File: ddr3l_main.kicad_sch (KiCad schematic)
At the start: 1 part

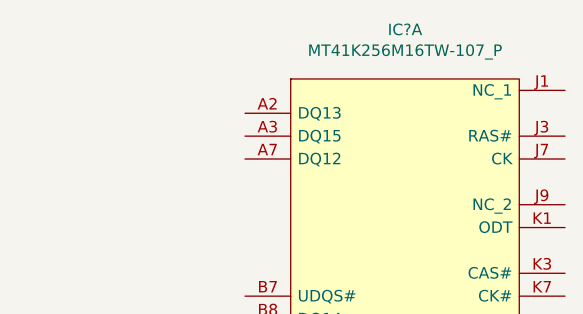
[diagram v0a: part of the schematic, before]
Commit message: Annotate symbols on ddr3l page
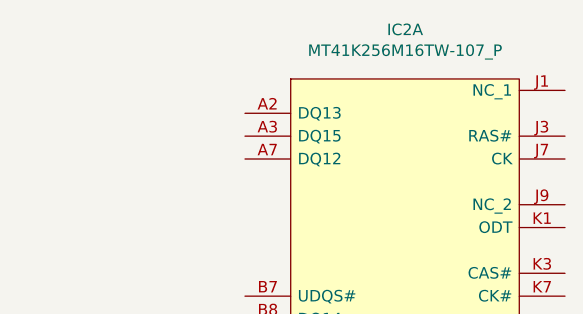
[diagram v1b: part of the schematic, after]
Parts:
- gave numbers to parts that had none: 1
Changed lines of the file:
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@@
 		(on_board yes)
 		(dnp no)
-		(property "Reference" "IC?"
+		(property "Reference" "IC2"
 			(at 99.06 35.179 0)
 			(effects
@@
 			(project "Simple_SDR"
 				(path "/006caa78-17ed-4ca3-959e-671c147c0629/00000000-0000-0000-0000-0000675f7864"
-					(reference "IC?")
+					(reference "IC2")
 					(unit 1)
 				)
